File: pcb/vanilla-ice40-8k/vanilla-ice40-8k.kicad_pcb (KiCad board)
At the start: 6 copper layers, 50 x 50 mm, 109 parts, among them J11 QSH-060-01-L-D-A, J12 QSH-060-01-L-D-A, J8 Conn_01x02_Pin, U1 ICE40HX8K-CT256, U2 W25X40CLSN, U3 FT2232HQ, U4 93LCxxBxxOT, U5 TPS563252DRLR, U6 TPS563252DRLR, X1 SG-8101CE 100Mhz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

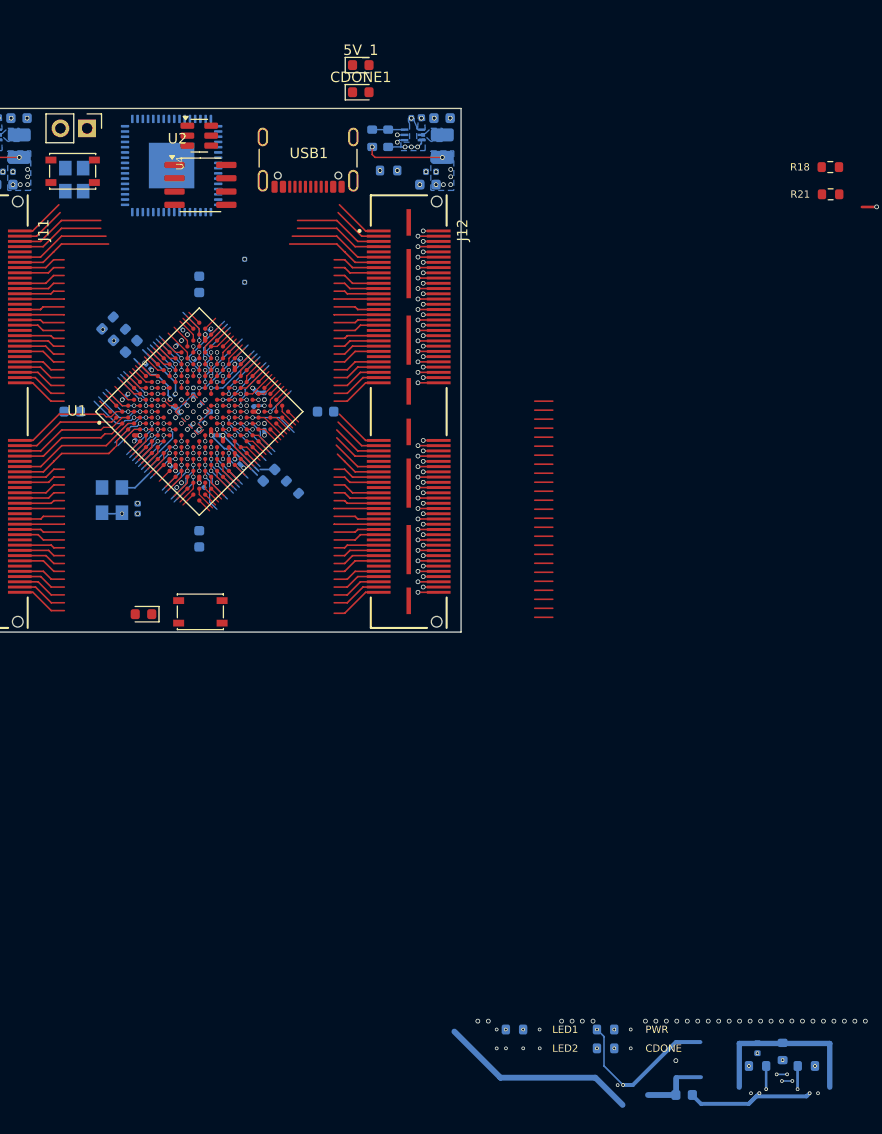
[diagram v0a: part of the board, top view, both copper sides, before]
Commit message: [hx8k][pcb] routed usb
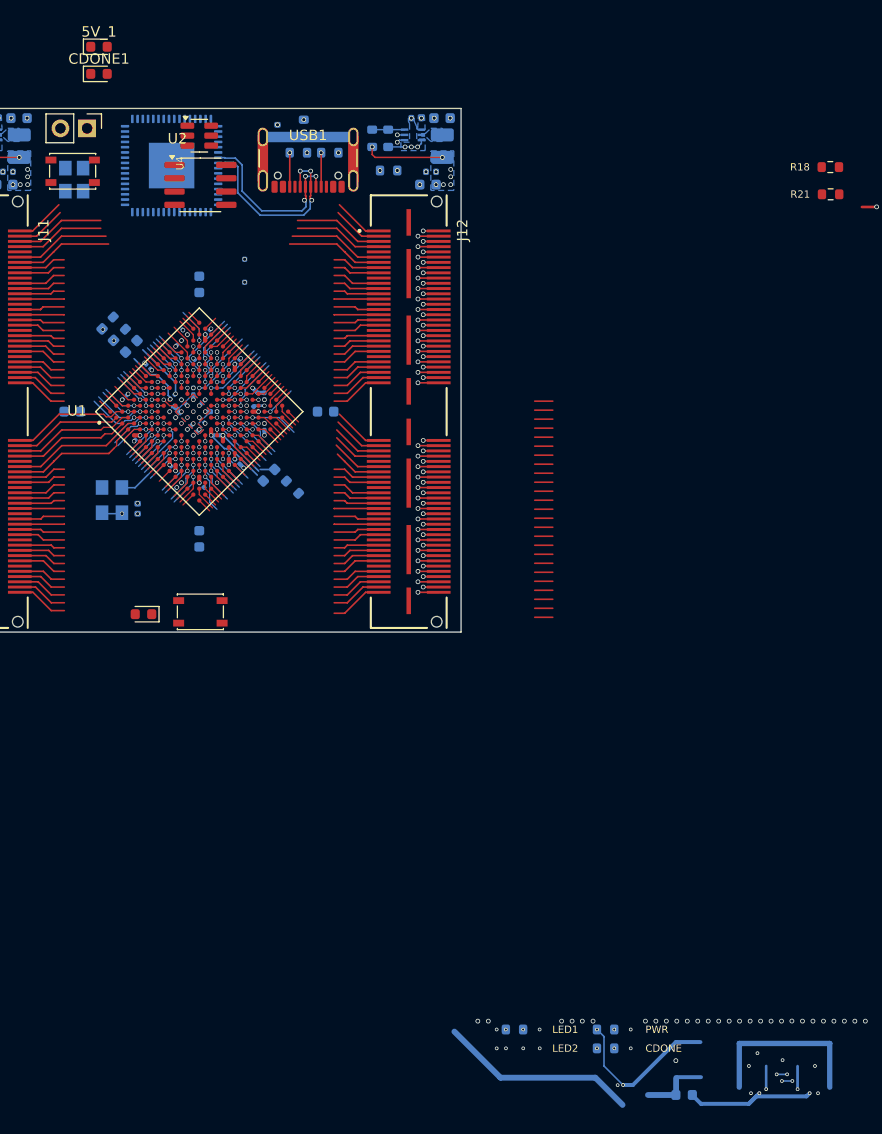
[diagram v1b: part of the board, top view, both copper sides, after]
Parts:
- moved R34 99.3 mm to (85.0, 48.0), turned to 90 degrees
- moved C51 98.9 mm to (82.5, 48.1), turned to -90 degrees
- moved R32 98.4 mm to (87.5, 50.3)
- moved R31 97.6 mm to (84.5, 50.3), turned to 180 degrees
- moved 5V_1 25.1 mm to (65.4, 40.2)
- moved CDONE1 25.1 mm to (65.4, 42.8)
- turned U3 to 180 degrees
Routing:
- net /USB_DP: track 1.88 -> 20.7 mm, vias 3 -> 6
- net /USB_DN: track 1.93 -> 19.1 mm, vias 3 -> 6
- net Net-(USB1-SHIELD): track 17.0 -> 34.0 mm
- net Net-(USB1-CC2): track 2.22 -> 5.47 mm, vias 1 -> 2
- net Net-(USB1-CC1): track 2.21 -> 5.46 mm, vias 1 -> 2
- net GND: vias 125 -> 129

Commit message: [hx8k][pcb] alignment marks for io tracks
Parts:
- FB3, R3, R6, R7: moved to F.Cu
- moved FB3 113.0 mm to (44.1, 57.7), turned to 0 degrees
- moved R6 107.0 mm to (38.0, 60.3)
- moved R7 104.0 mm to (38.0, 62.8), turned to 0 degrees
- moved R3 101.5 mm to (38.0, 57.7)
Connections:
- J11 pad 5: /IOT_190 -> /IOT_173
- J11 pad 7: /IOT_173 -> /IOT_190
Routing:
- net (no net): track 79.6 -> 22.1 mm, vias 7 -> 5
- net EXT_5V: track 19.0 -> 0.00 mm
- net /IOR_140_USR1: track 18.3 -> 0.00 mm, vias 1 -> 0
- net Net-(USB1-SHIELD): track 34.0 -> 17.0 mm
- net /CDONE: track 21.6 -> 5.31 mm, vias 2 -> 1
- net +5V: track 16.1 -> 0.70 mm, vias 8 -> 5
- net Net-(FB3-Pad1): track 13.4 -> 0.00 mm, vias 2 -> 0
- net USB_5V: track 6.69 -> 0.00 mm
- net Net-(USB1-CC2): track 5.47 -> 3.25 mm, vias 2 -> 1
- net Net-(USB1-CC1): track 5.46 -> 3.25 mm, vias 2 -> 1
- net /IOB_100: track 7.91 -> 6.19 mm
- net /USB_DN: track 19.1 -> 18.1 mm, vias 6 -> 4
- net /USB_DP: track 20.7 -> 19.8 mm, vias 6 -> 4
- net /IOT_190: track 6.01 -> 6.69 mm, vias 2 -> 3
- net /IOT_173: track 7.28 -> 6.78 mm
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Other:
- board text removed: "CDONE"
- board text removed: "LED1"
- board text removed: "LED2"
- board text removed: "PWR"

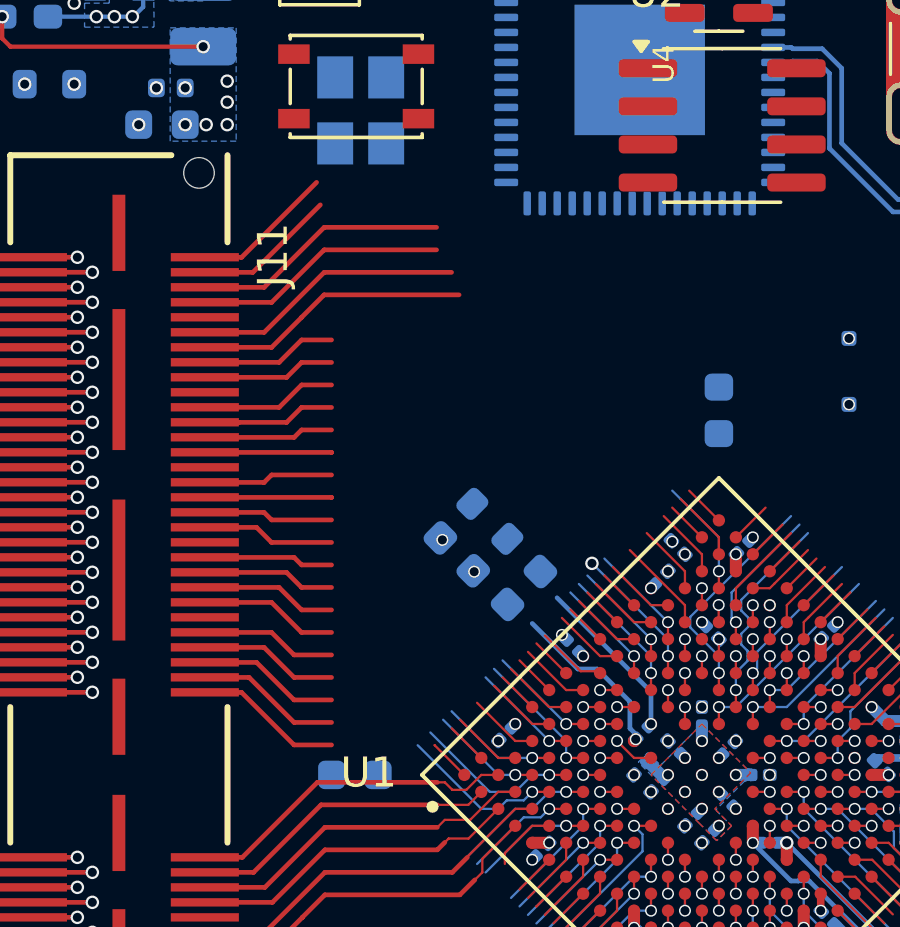
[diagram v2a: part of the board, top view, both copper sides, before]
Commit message: [hx8k][pcb] upper j1 partial routing
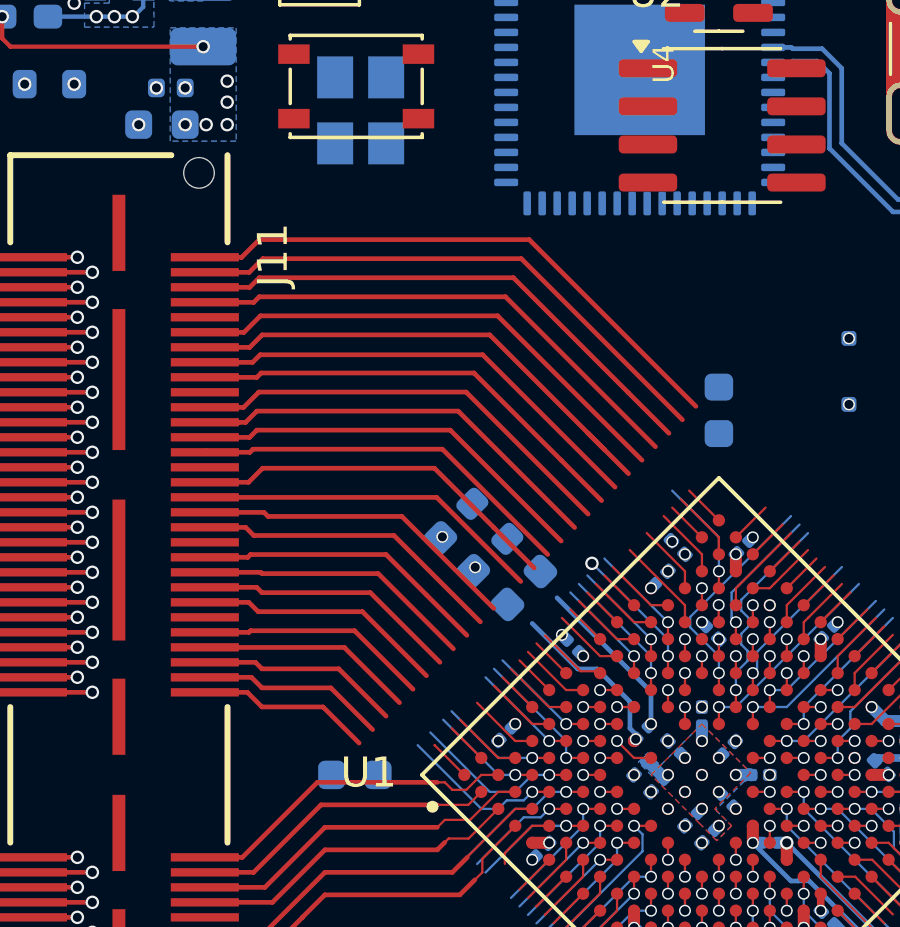
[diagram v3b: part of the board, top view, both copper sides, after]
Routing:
- net /IOT_170: track 9.36 -> 23.5 mm
- net /IOT_176: track 6.21 -> 19.8 mm
- net /IOT_172: track 7.73 -> 18.8 mm
- net /IOT_182: track 6.82 -> 17.4 mm
- net /IOT_187: track 5.95 -> 16.1 mm
- net /IOT_184: track 7.98 -> 17.6 mm
- net /IOT_169: track 10.9 -> 20.1 mm
- net /IOT_186: track 5.75 -> 14.9 mm
- net /IOT_183: track 6.62 -> 15.4 mm
- net /IOT_177: track 9.87 -> 18.6 mm
- net /IOT_194: track 5.75 -> 14.0 mm
- net /IOT_178: track 11.6 -> 19.4 mm
- net /IOT_171: track 11.4 -> 19.2 mm
- net /IOT_199: track 6.62 -> 14.1 mm
- net /IOT_203: track 6.63 -> 13.3 mm
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
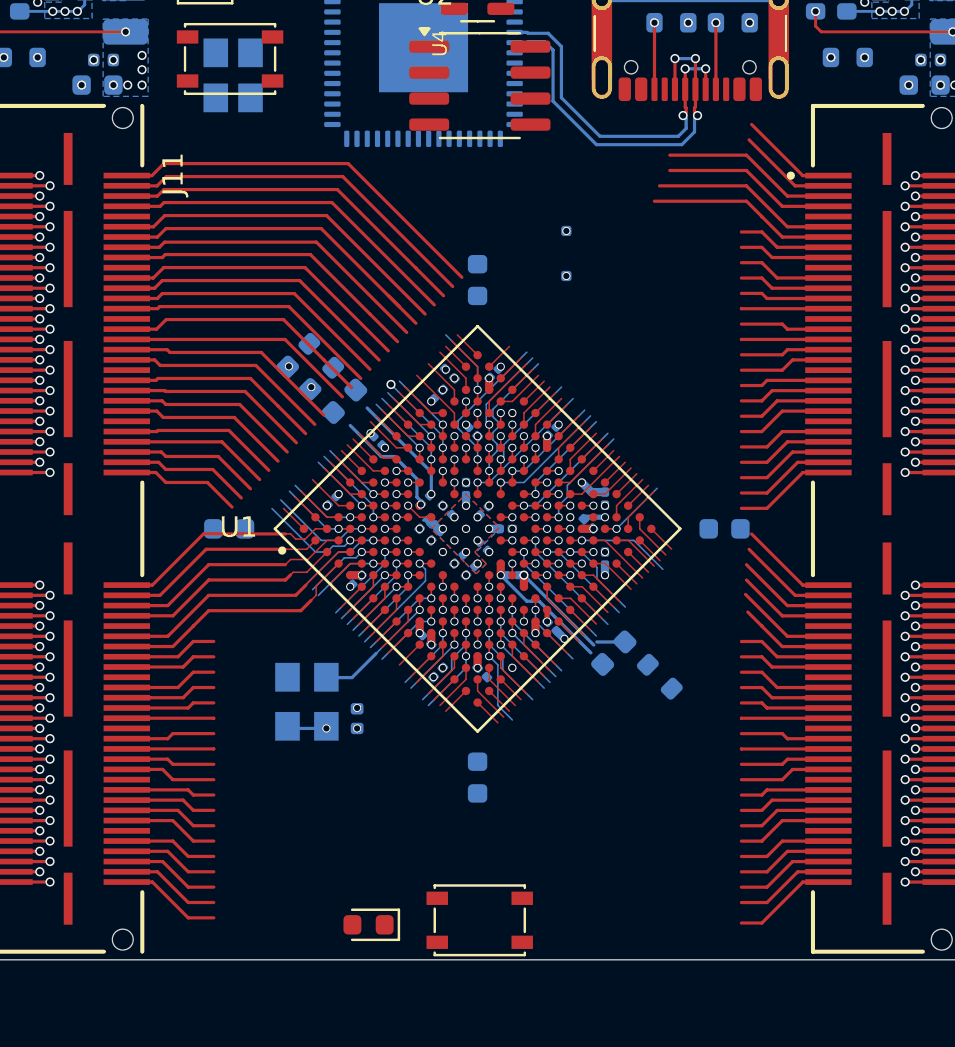
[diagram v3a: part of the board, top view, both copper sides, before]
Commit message: [hx8k][pcb] j1 and j2 top layer initial routing
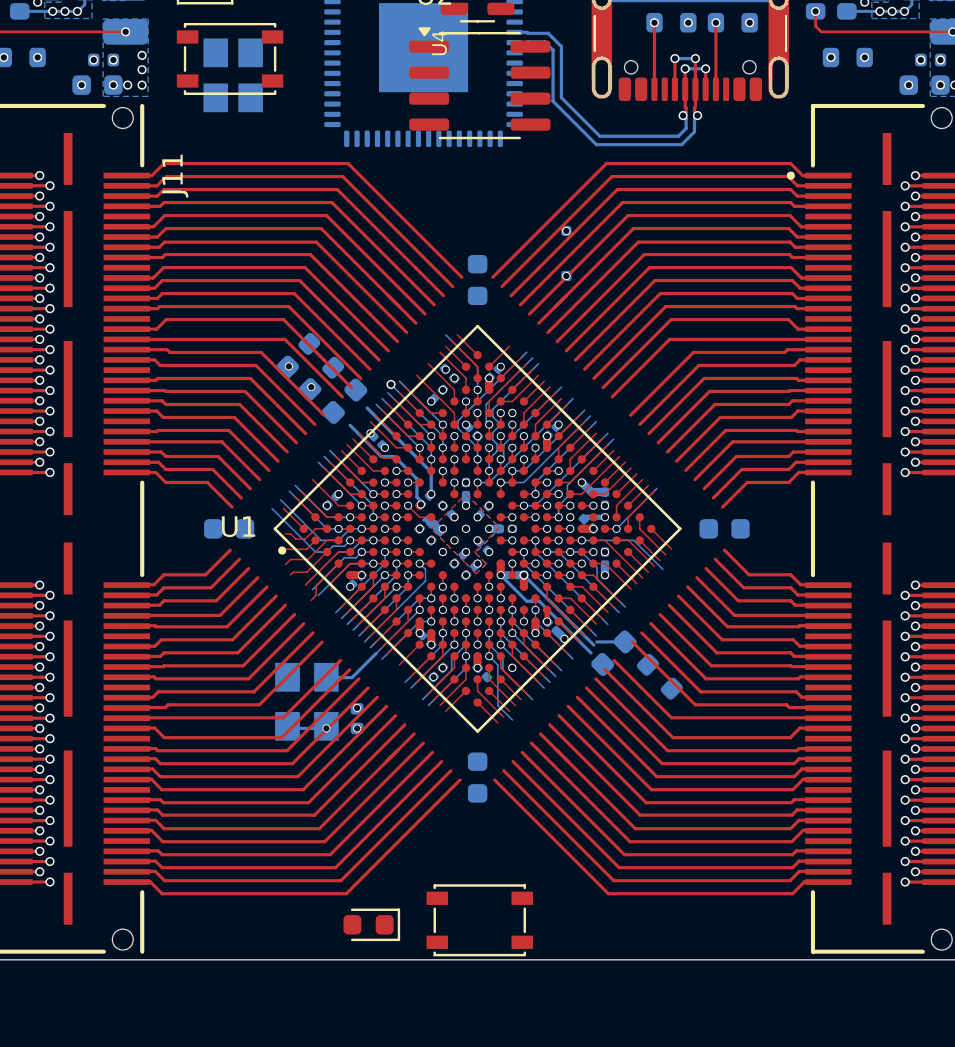
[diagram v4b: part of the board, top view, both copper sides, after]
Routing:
- net unconnected-(J12-Pad109): track 0.00 -> 16.8 mm
- net unconnected-(J11-Pad110): track 0.00 -> 16.8 mm
- net /IOT_171: track 19.2 -> 36.0 mm
- net unconnected-(J12-Pad99): track 0.00 -> 14.7 mm
- net /IOT_187: track 16.1 -> 30.8 mm
- net /IOR_165: track 6.19 -> 20.3 mm
- net /IOL_25B: track 11.3 -> 25.2 mm
- net /IOB_53: track 6.48 -> 20.3 mm
- net /IOR_161: track 6.21 -> 19.8 mm
- net /IOT_186: track 14.9 -> 28.5 mm
- net /IOL_23B: track 8.60 -> 22.1 mm
- net /IOB_55: track 7.24 -> 20.7 mm
- net /IOL_26A: track 6.17 -> 19.2 mm
- net /IOB_57: track 6.17 -> 19.2 mm
- net unconnected-(J12-Pad89): track 0.00 -> 12.6 mm
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
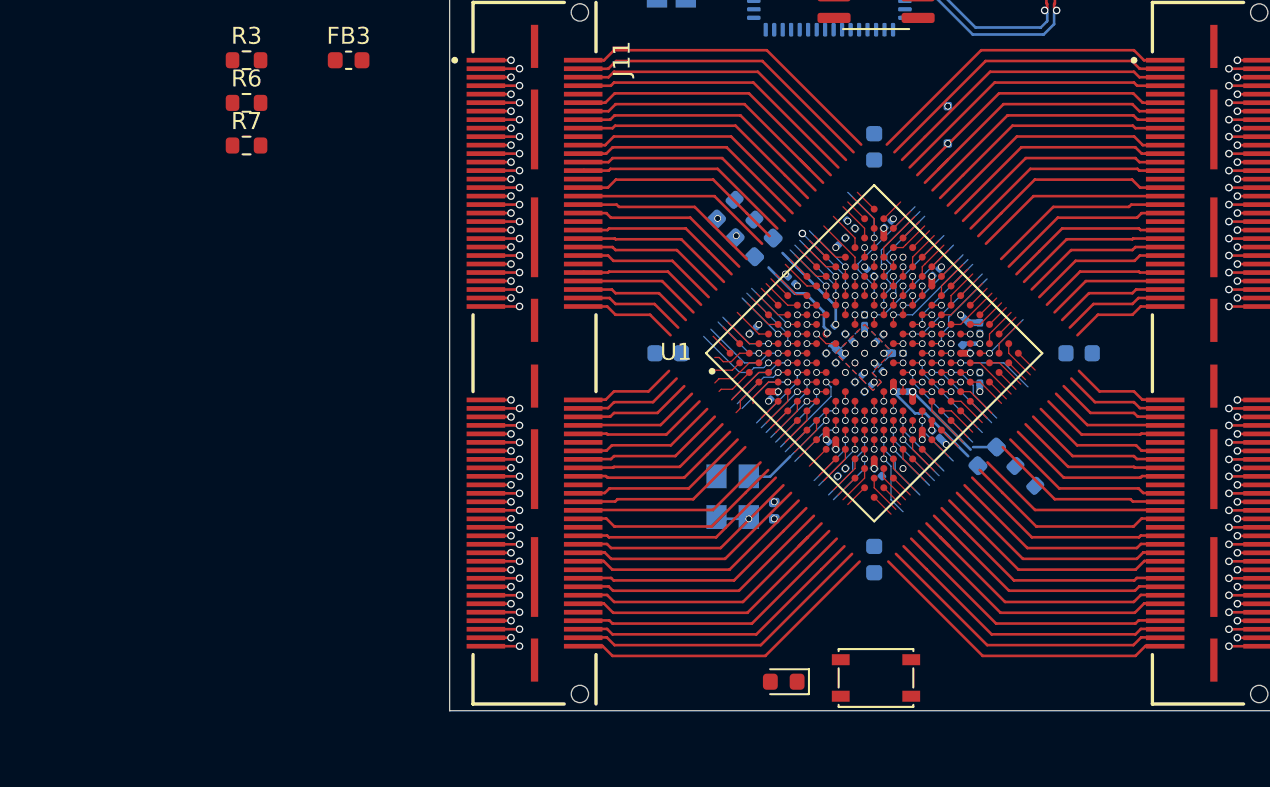
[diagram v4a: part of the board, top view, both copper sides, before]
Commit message: [hx8k][pcb] lower j1 and j2 redo in progress
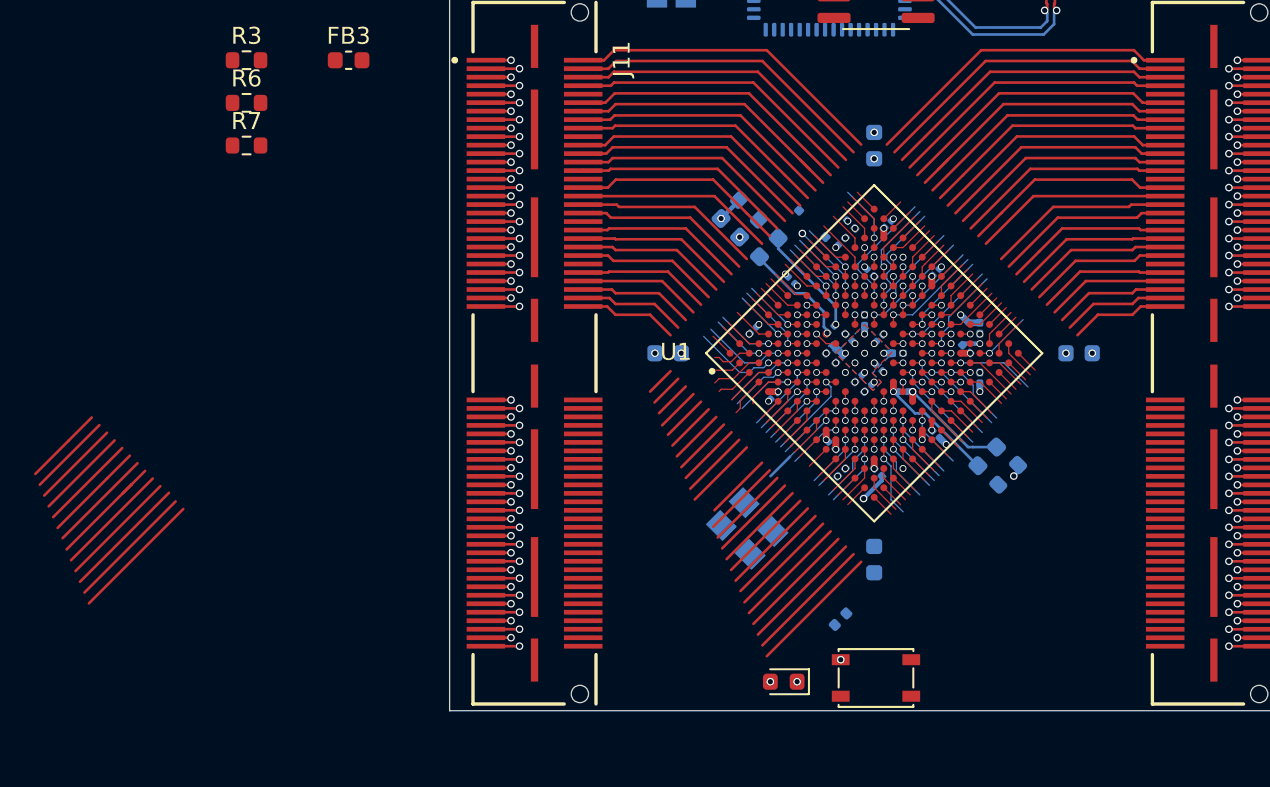
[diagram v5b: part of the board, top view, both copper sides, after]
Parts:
- moved C20 10.0 mm to (75.0, 62.8), turned to 90 degrees
- moved D1 9.88 mm to (71.4, 67.4), turned to 135 degrees
- moved C2 9.72 mm to (66.5, 67.6), turned to -45 degrees
- moved C1 7.49 mm to (73.0, 90.7), turned to -135 degrees
- moved X1 2.06 mm to (67.5, 85.3), turned to 135 degrees
- moved R10 1.01 mm to (82.9, 82.2), turned to -135 degrees
- moved C12 0.29 mm to (68.8, 68.8)
- moved R11 0.26 mm to (67.6, 66.5)
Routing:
- net +1V2: track 8.13 -> 133.2 mm, vias 15 -> 17
- net /IOB_53: track 20.3 -> 1.40 mm
- net /IOB_55: track 20.7 -> 2.37 mm
- net /IOB_57: track 19.2 -> 1.40 mm
- net /IOB_59: track 19.6 -> 2.37 mm
- net /IOB_63: track 19.4 -> 2.37 mm
- net unconnected-(J12-Pad109): track 16.8 -> 0.00 mm
- net /IOT_171: track 36.0 -> 19.2 mm
- net /IOR_157: track 2.37 -> 19.2 mm
- net /IOB_60: track 18.0 -> 2.37 mm
- net /IOB_73: track 16.7 -> 1.40 mm
- net /IOB_69: track 16.5 -> 1.40 mm
- net unconnected-(J12-Pad99): track 14.7 -> 0.00 mm
- net /IOT_187: track 30.8 -> 16.1 mm
- net /IOB_75: track 14.9 -> 1.40 mm
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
